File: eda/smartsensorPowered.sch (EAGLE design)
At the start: 36 parts, among them Q1 IRFML8244, Q2 IRFML8244, Q3 IRFML8244, Q4 IRFML8244, U1 ISL83491SOIC, U2 ATTINY1634

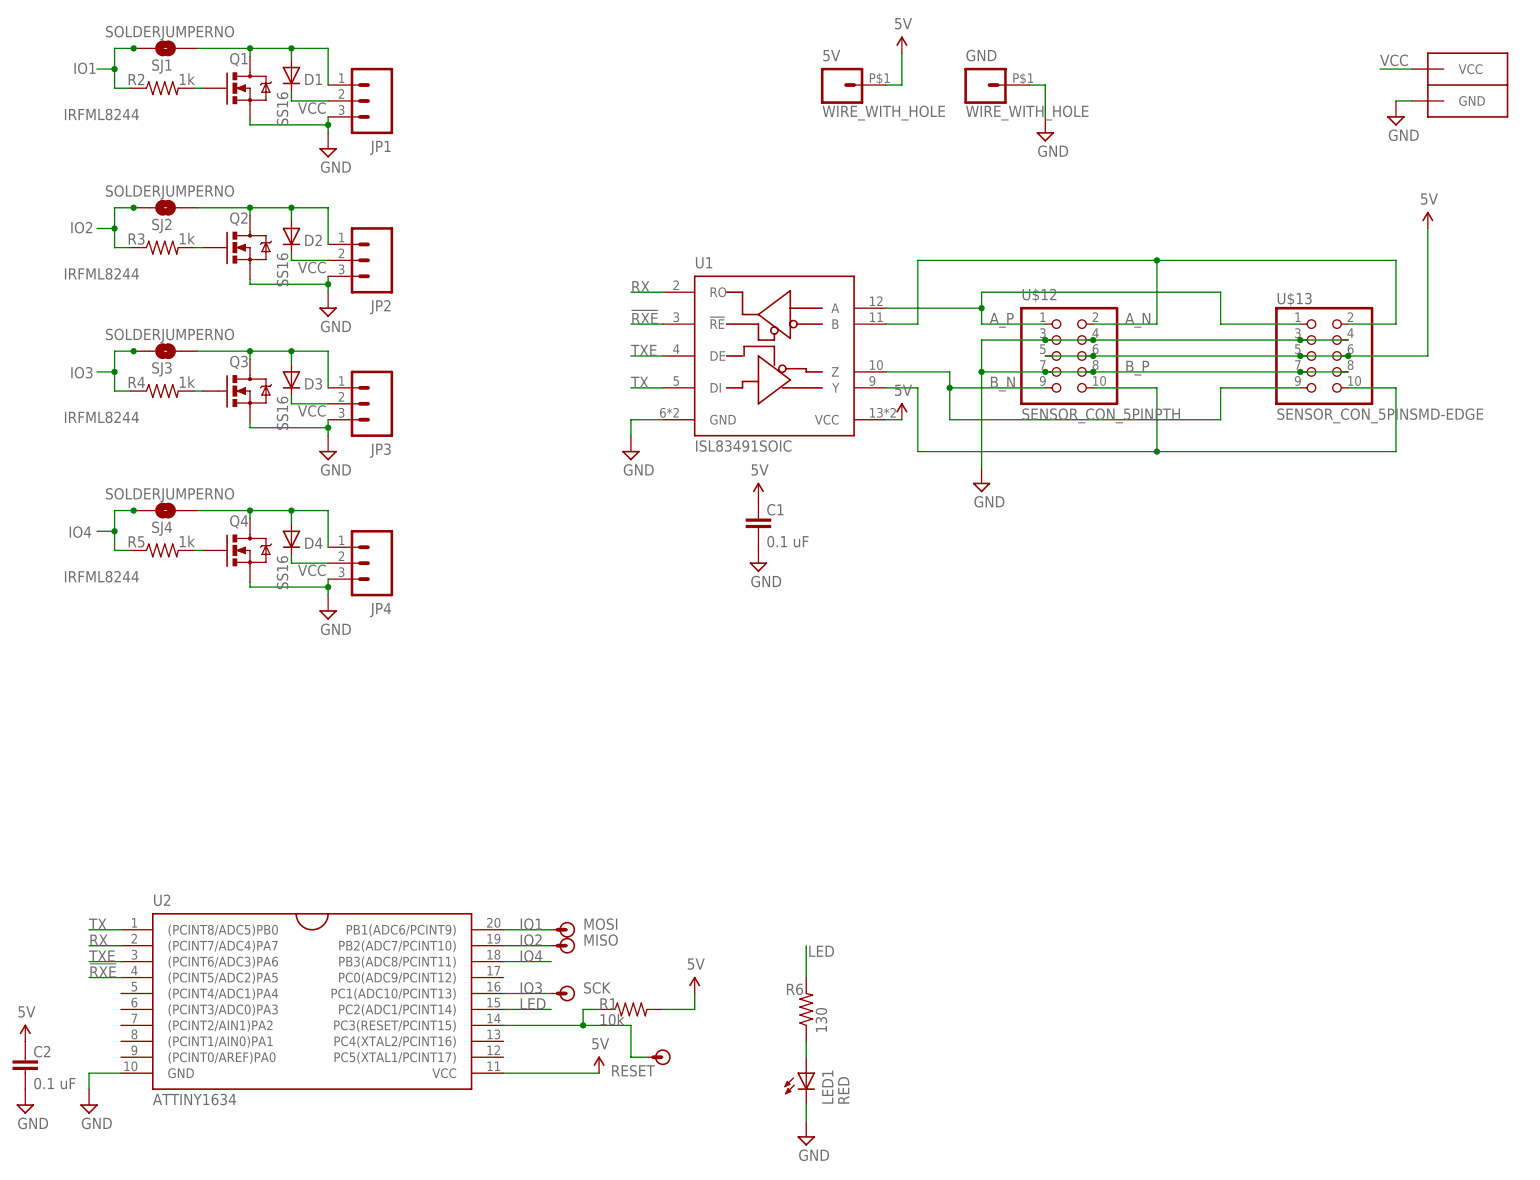
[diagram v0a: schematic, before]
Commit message: Rerouted to accomodate 2x5 shrouded connector. On battery_buzzer, grizzly_bear, smartsensor, smartsensor_powered, and team_flag. Thanks Doug and Yizhe for helping!
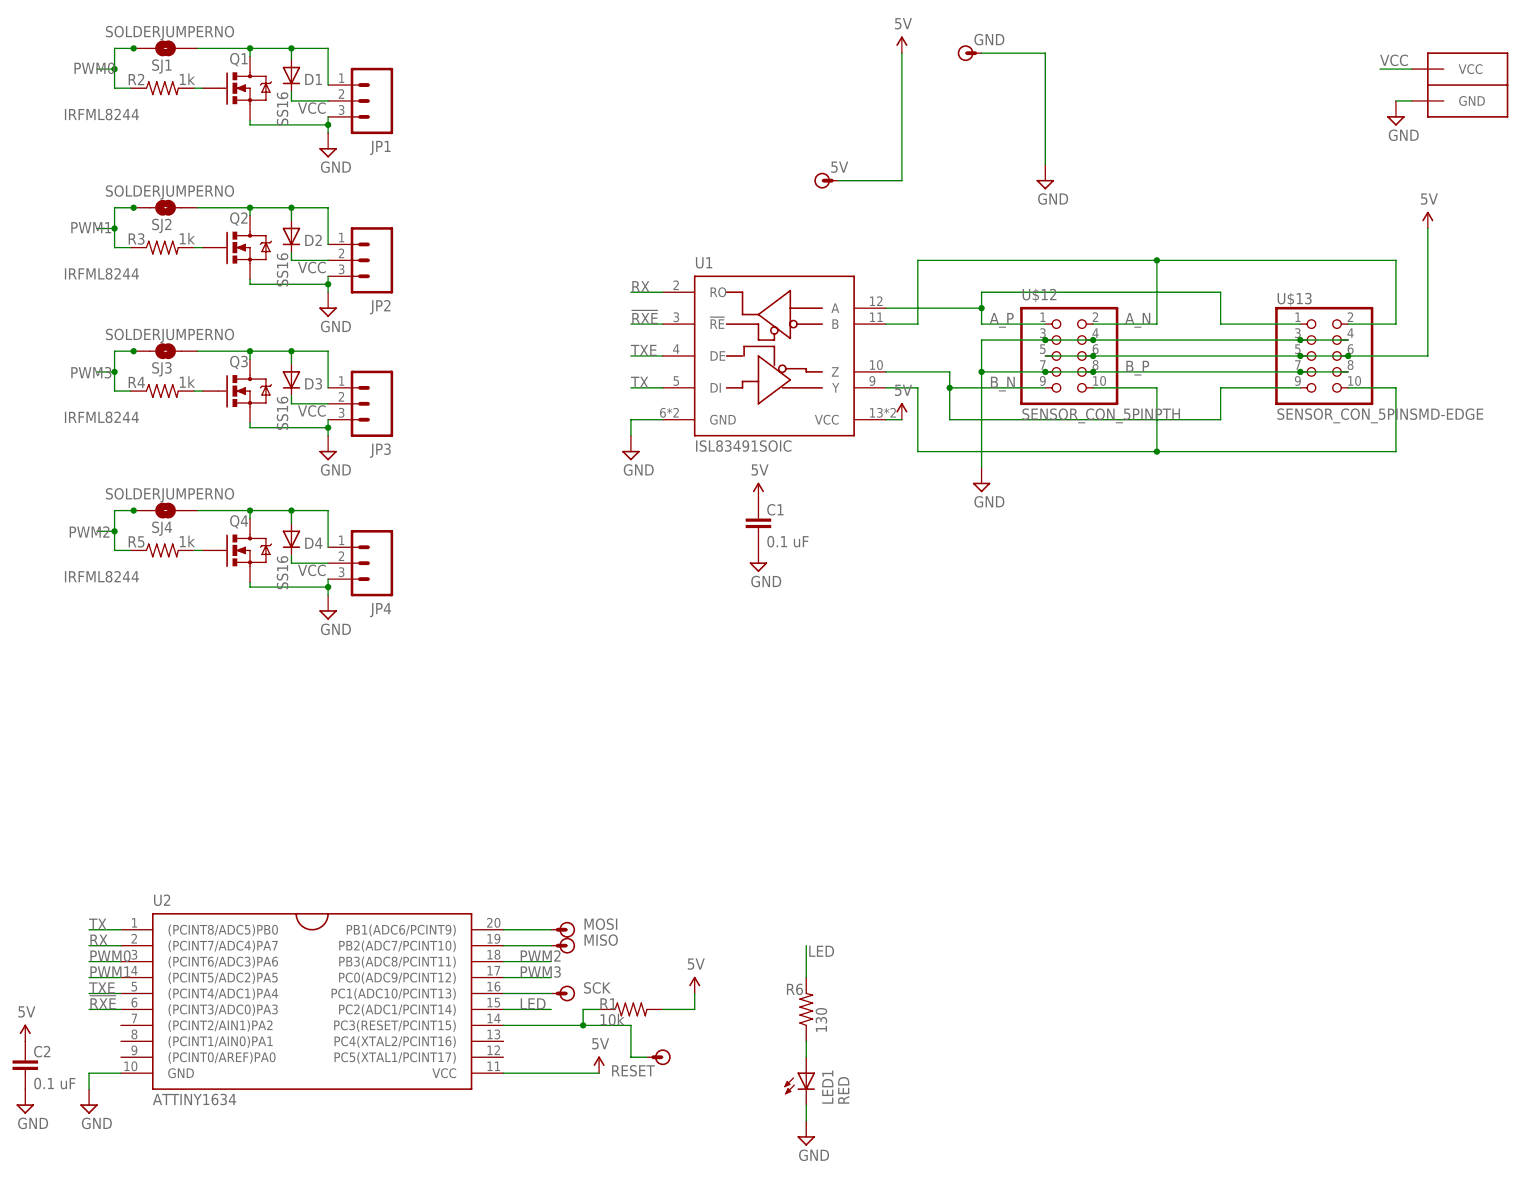
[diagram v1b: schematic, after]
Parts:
- 5V, GND: value WIRE_WITH_HOLE -> (none); device pie:WIRE_WITH_HOLE -> pie:POGO_PIN
- U$12: device pie:SENSOR_CON_5PINPTH -> pie:SENSOR_CON_5PINPTH-SHROUDED
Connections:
- net IO4 renamed PWM2
- removed net IO1: MOSI.P$1, R2.1, SJ1.1, U2.PB1(ADC6/PCINT9)
- removed net IO2: MISO.P$1, R3.1, SJ2.1, U2.PB2(ADC7/PCINT10)
- removed net IO3: R4.1, SCK.P$1, SJ3.1, U2.PC1(ADC10/PCINT13)
- new net N$12: SCK.P$1, U2.PC1(ADC10/PCINT13)
- new net N$6: MOSI.P$1, U2.PB1(ADC6/PCINT9)
- new net N$9: MISO.P$1, U2.PB2(ADC7/PCINT10)
- new net PWM0: R2.1, SJ1.1, U2.(PCINT6/ADC3)PA6
- new net PWM1: R3.1, SJ2.1, U2.(PCINT5/ADC2)PA5
- new net PWM3: R4.1, SJ3.1, U2.PC0(ADC9/PCINT12)
- net !RXE: now also U2.(PCINT3/ADC0)PA3; no longer U2.(PCINT5/ADC2)PA5
- net 5V: now also 5V.P$1; no longer 5V.2
- net GND: now also GND.P$1; no longer GND.2
- net TXE: now also U2.(PCINT4/ADC1)PA4; no longer U2.(PCINT6/ADC3)PA6
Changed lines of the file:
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@@
 <part name="R1" library="pie" deviceset="R-US_" device="R0603" value="10k"/>
 <part name="U$6" library="pie" deviceset="5V" device=""/>
-<part name="GND" library="pie" deviceset="WIRE_WITH_HOLE" device=""/>
-<part name="5V" library="pie" deviceset="WIRE_WITH_HOLE" device=""/>
 <part name="U$16" library="pie" deviceset="5V" device=""/>
 <part name="SUPPLY6" library="pie" deviceset="GND" device=""/>
@@
 <part name="SUPPLY12" library="pie" deviceset="GND" device=""/>
 <part name="U$11" library="pie" deviceset="5V" device=""/>
-<part name="U$12" library="pie" deviceset="SENSOR_CON_5PIN" device="PTH" value="SENSOR_CON_5PINPTH"/>
+<part name="U$12" library="pie" deviceset="SENSOR_CON_5PIN" device="PTH-SHROUDED" value="SENSOR_CON_5PINPTH"/>
 <part name="U$13" library="pie" deviceset="SENSOR_CON_5PIN" device="SMD-EDGE" value="SENSOR_CON_5PINSMD-EDGE"/>
 <part name="SUPPLY13" library="pie" deviceset="GND" device=""/>
@@
 <part name="SCK" library="pie" deviceset="POGO_PIN" device=""/>
 <part name="U$8" library="pie" deviceset="5V" device=""/>
+<part name="5V" library="pie" deviceset="POGO_PIN" device=""/>
+<part name="GND" library="pie" deviceset="POGO_PIN" device=""/>
 </parts>
 <sheets>
@@
 </instance>
 <instance part="U$6" gate="G$1" x="111.76" y="27.94"/>
-<instance part="GND" gate="G$1" x="157.48" y="172.72"/>
-<instance part="5V" gate="G$1" x="134.62" y="172.72"/>
 <instance part="U$16" gate="G$1" x="144.78" y="177.8"/>
-<instance part="SUPPLY6" gate="GND" x="167.64" y="165.1"/>
+<instance part="SUPPLY6" gate="GND" x="167.64" y="157.48"/>
 <instance part="SUPPLY10" gate="GND" x="53.34" y="162.56"/>
 <instance part="Q1" gate="G$1" x="40.894" y="172.212" smashed="yes">
@@
 </instance>
 <instance part="U$8" gate="G$1" x="228.6" y="149.86"/>
+<instance part="5V" gate="G$1" x="132.08" y="157.48"/>
+<instance part="GND" gate="G$1" x="154.94" y="177.8"/>
 </instances>
 <busses>
@@
 </segment>
 <segment>
-<wire x1="142.24" y1="172.72" x2="144.78" y2="172.72" width="0.1524" layer="91"/>
 <pinref part="U$16" gate="G$1" pin="5V"/>
-<wire x1="144.78" y1="172.72" x2="144.78" y2="177.8" width="0.1524" layer="91"/>
-<pinref part="5V" gate="G$1" pin="2"/>
+<wire x1="144.78" y1="177.8" x2="144.78" y2="157.48" width="0.1524" layer="91"/>
+<pinref part="5V" gate="G$1" pin="P$1"/>
+<wire x1="144.78" y1="157.48" x2="134.62" y2="157.48" width="0.1524" layer="91"/>
 </segment>
 <segment>
@@
 </segment>
 <segment>
-<wire x1="165.1" y1="172.72" x2="167.64" y2="172.72" width="0.1524" layer="91"/>
 <pinref part="SUPPLY6" gate="GND" pin="GND"/>
-<wire x1="167.64" y1="172.72" x2="167.64" y2="167.64" width="0.1524" layer="91"/>
-<pinref part="GND" gate="G$1" pin="2"/>
+<pinref part="GND" gate="G$1" pin="P$1"/>
+<wire x1="157.48" y1="177.8" x2="167.64" y2="177.8" width="0.1524" layer="91"/>
+<wire x1="167.64" y1="177.8" x2="167.64" y2="160.02" width="0.1524" layer="91"/>
 </segment>
 <segment>
@@
 <net name="TXE" class="0">
 <segment>
-<pinref part="U2" gate="G$1" pin="(PCINT6/ADC3)PA6"/>
-<wire x1="20.32" y1="33.02" x2="15.24" y2="33.02" width="0.1524" layer="91"/>
-<label x="15.24" y="33.02" size="1.778" layer="95"/>
-</segment>
-<segment>
 <pinref part="U1" gate="G$1" pin="DE"/>
 <wire x1="106.68" y1="129.54" x2="101.6" y2="129.54" width="0.1524" layer="91"/>
 <label x="101.6" y="129.54" size="1.778" layer="95"/>
 </segment>
+<segment>
+<pinref part="U2" gate="G$1" pin="(PCINT4/ADC1)PA4"/>
+<wire x1="20.32" y1="27.94" x2="15.24" y2="27.94" width="0.1524" layer="91"/>
+<label x="15.24" y="27.94" size="1.778" layer="95"/>
+</segment>
 </net>
 <net name="!RXE" class="0">
-<segment>
-<pinref part="U2" gate="G$1" pin="(PCINT5/ADC2)PA5"/>
-<wire x1="20.32" y1="30.48" x2="15.24" y2="30.48" width="0.1524" layer="91"/>
-<label x="15.24" y="30.48" size="1.778" layer="95"/>
-</segment>
 <segment>
 <pinref part="U1" gate="G$1" pin="!RE"/>
 <wire x1="106.68" y1="134.62" x2="101.6" y2="134.62" width="0.1524" layer="91"/>
 <label x="101.6" y="134.62" size="1.778" layer="95"/>
+</segment>
+<segment>
+<pinref part="U2" gate="G$1" pin="(PCINT3/ADC0)PA3"/>
+<wire x1="20.32" y1="25.4" x2="15.24" y2="25.4" width="0.1524" layer="91"/>
+<label x="15.24" y="25.4" size="1.778" layer="95"/>
 </segment>
 </net>
@@
 </segment>
 </net>
-<net name="IO1" class="0">
-<segment>
-<pinref part="U2" gate="G$1" pin="PB1(ADC6/PCINT9)"/>
-<wire x1="81.28" y1="38.1" x2="88.9" y2="38.1" width="0.1524" layer="91"/>
-<label x="83.82" y="38.1" size="1.778" layer="95"/>
-<pinref part="MOSI" gate="G$1" pin="P$1"/>
-</segment>
+<net name="PWM0" class="0">
 <segment>
 <wire x1="22.606" y1="178.562" x2="22.352" y2="178.562" width="0.1524" layer="91"/>
@@
 <label x="12.7" y="174.498" size="1.778" layer="95"/>
 </segment>
-</net>
-<net name="IO2" class="0">
-<segment>
-<pinref part="U2" gate="G$1" pin="PB2(ADC7/PCINT10)"/>
-<wire x1="81.28" y1="35.56" x2="88.9" y2="35.56" width="0.1524" layer="91"/>
-<label x="83.82" y="35.56" size="1.778" layer="95"/>
-<pinref part="MISO" gate="G$1" pin="P$1"/>
-</segment>
+<segment>
+<pinref part="U2" gate="G$1" pin="(PCINT6/ADC3)PA6"/>
+<wire x1="20.32" y1="33.02" x2="15.24" y2="33.02" width="0.1524" layer="91"/>
+<label x="15.24" y="33.02" size="1.778" layer="95"/>
+</segment>
+</net>
+<net name="PWM1" class="0">
 <segment>
 <wire x1="22.606" y1="153.162" x2="22.352" y2="153.162" width="0.1524" layer="91"/>
@@
 <label x="12.192" y="149.098" size="1.778" layer="95"/>
 </segment>
-</net>
-<net name="IO3" class="0">
-<segment>
-<pinref part="U2" gate="G$1" pin="PC1(ADC10/PCINT13)"/>
-<wire x1="81.28" y1="27.94" x2="88.9" y2="27.94" width="0.1524" layer="91"/>
-<label x="83.82" y="27.94" size="1.778" layer="95"/>
-<pinref part="SCK" gate="G$1" pin="P$1"/>
-</segment>
+<segment>
+<pinref part="U2" gate="G$1" pin="(PCINT5/ADC2)PA5"/>
+<wire x1="20.32" y1="30.48" x2="15.24" y2="30.48" width="0.1524" layer="91"/>
+<label x="15.24" y="30.48" size="1.778" layer="95"/>
+</segment>
+</net>
+<net name="PWM3" class="0">
 <segment>
 <wire x1="22.606" y1="130.302" x2="22.352" y2="130.302" width="0.1524" layer="91"/>
@@
 <label x="12.192" y="125.984" size="1.778" layer="95"/>
 </segment>
-</net>
-<net name="IO4" class="0">
-<segment>
-<pinref part="U2" gate="G$1" pin="PB3(ADC8/PCINT11)"/>
-<wire x1="81.28" y1="33.02" x2="88.9" y2="33.02" width="0.1524" layer="91"/>
-<label x="83.82" y="33.02" size="1.778" layer="95"/>
-</segment>
-<segment>
-<wire x1="22.606" y1="104.902" x2="22.352" y2="104.902" width="0.1524" layer="91"/>
-<wire x1="22.352" y1="104.902" x2="19.304" y2="104.902" width="0.1524" layer="91"/>
-<wire x1="19.304" y1="104.902" x2="19.304" y2="101.6" width="0.1524" layer="91"/>
-<pinref part="R5" gate="G$1" pin="1"/>
-<wire x1="19.304" y1="101.6" x2="19.304" y2="98.552" width="0.1524" layer="91"/>
-<wire x1="19.304" y1="98.552" x2="21.844" y2="98.552" width="0.1524" layer="91"/>
-<wire x1="19.304" y1="101.6" x2="16.51" y2="101.6" width="0.1524" layer="91"/>
-<junction x="19.304" y="101.6"/>
-<pinref part="SJ4" gate="1" pin="1"/>
-<junction x="22.352" y="104.902"/>
-<label x="11.938" y="100.584" size="1.778" layer="95"/>
+<segment>
+<pinref part="U2" gate="G$1" pin="PC0(ADC9/PCINT12)"/>
+<wire x1="81.28" y1="30.48" x2="88.9" y2="30.48" width="0.1524" layer="91"/>
+<label x="83.82" y="30.48" size="1.778" layer="95"/>
 </segment>
 </net>
@@
 </segment>
 </net>
+<net name="PWM2" class="0">
+<segment>
+<pinref part="U2" gate="G$1" pin="PB3(ADC8/PCINT11)"/>
+<wire x1="81.28" y1="33.02" x2="88.9" y2="33.02" width="0.1524" layer="91"/>
+<label x="83.82" y="33.02" size="1.778" layer="95"/>
+</segment>
+<segment>
+<wire x1="22.606" y1="104.902" x2="22.352" y2="104.902" width="0.1524" layer="91"/>
+<wire x1="22.352" y1="104.902" x2="19.304" y2="104.902" width="0.1524" layer="91"/>
+<wire x1="19.304" y1="104.902" x2="19.304" y2="101.6" width="0.1524" layer="91"/>
+<pinref part="R5" gate="G$1" pin="1"/>
+<wire x1="19.304" y1="101.6" x2="19.304" y2="98.552" width="0.1524" layer="91"/>
+<wire x1="19.304" y1="98.552" x2="21.844" y2="98.552" width="0.1524" layer="91"/>
+<wire x1="19.304" y1="101.6" x2="16.51" y2="101.6" width="0.1524" layer="91"/>
+<junction x="19.304" y="101.6"/>
+<pinref part="SJ4" gate="1" pin="1"/>
+<junction x="22.352" y="104.902"/>
+<label x="11.938" y="100.584" size="1.778" layer="95"/>
+</segment>
+</net>
+<net name="N$6" class="0">
+<segment>
+<pinref part="U2" gate="G$1" pin="PB1(ADC6/PCINT9)"/>
+<pinref part="MOSI" gate="G$1" pin="P$1"/>
+<wire x1="81.28" y1="38.1" x2="88.9" y2="38.1" width="0.1524" layer="91"/>
+</segment>
+</net>
+<net name="N$9" class="0">
+<segment>
+<pinref part="MISO" gate="G$1" pin="P$1"/>
+<pinref part="U2" gate="G$1" pin="PB2(ADC7/PCINT10)"/>
+<wire x1="88.9" y1="35.56" x2="81.28" y2="35.56" width="0.1524" layer="91"/>
+</segment>
+</net>
+<net name="N$12" class="0">
+<segment>
+<pinref part="SCK" gate="G$1" pin="P$1"/>
+<pinref part="U2" gate="G$1" pin="PC1(ADC10/PCINT13)"/>
+<wire x1="88.9" y1="27.94" x2="81.28" y2="27.94" width="0.1524" layer="91"/>
+</segment>
+</net>
